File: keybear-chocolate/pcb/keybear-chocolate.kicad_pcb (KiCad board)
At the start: 2 copper layers, 136.9 x 98.2 mm, 97 parts, among them J1 MJ-4PP-9, J2 BATT, J3 LED, J4 OLED, SW1 SW_PUSH, SW10 SW_PUSH, SW11 SW_PUSH, SW12 SW_PUSH, SW13 SW_PUSH, SW14 SW_PUSH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

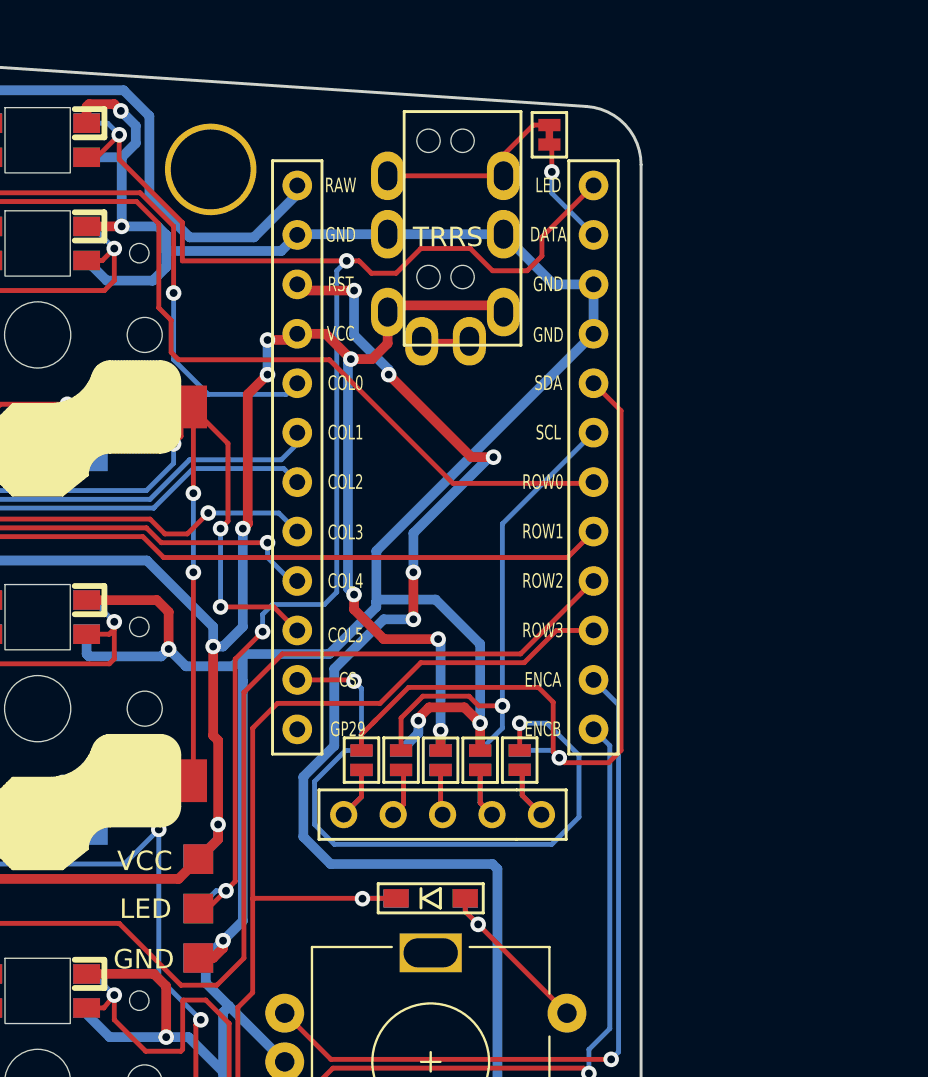
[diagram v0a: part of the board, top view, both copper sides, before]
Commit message: moving LED ping. Adding/rename RX/TX
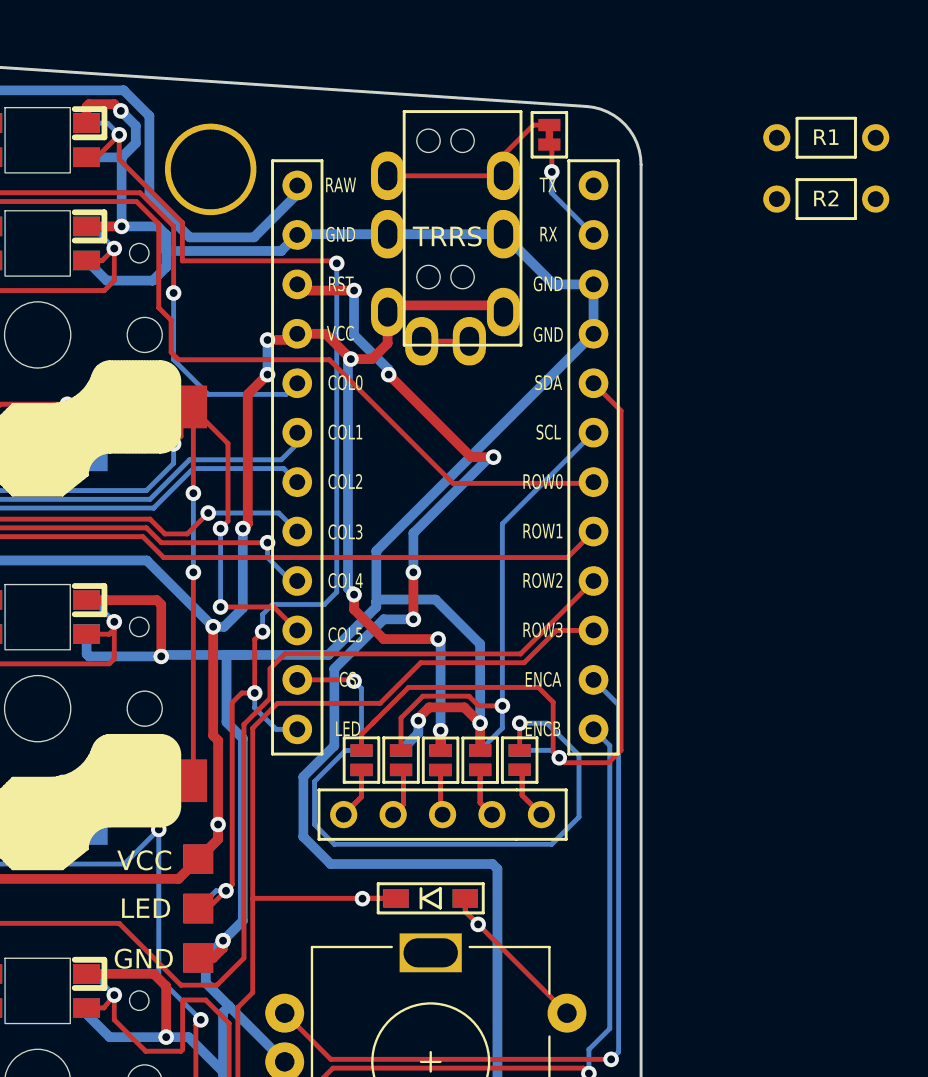
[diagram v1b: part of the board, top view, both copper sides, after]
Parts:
- added R1: R, SofleKeyboard-footprint:RESISTOR_mini, F.Cu at (286.5, 97.6)
- added R2: R, SofleKeyboard-footprint:RESISTOR_mini, F.Cu at (286.5, 100.7)
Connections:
- net data renamed RX
- U1 pad 1: LED -> TX
- U1 pad 13: unconnected-(U1-B6-Pad13) -> LED
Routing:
- net LED: track 77.4 -> 64.1 mm, vias 4 -> 5
- net VCC: track 875.4 -> 874.4 mm
- net GND: track 901.1 -> 901.9 mm

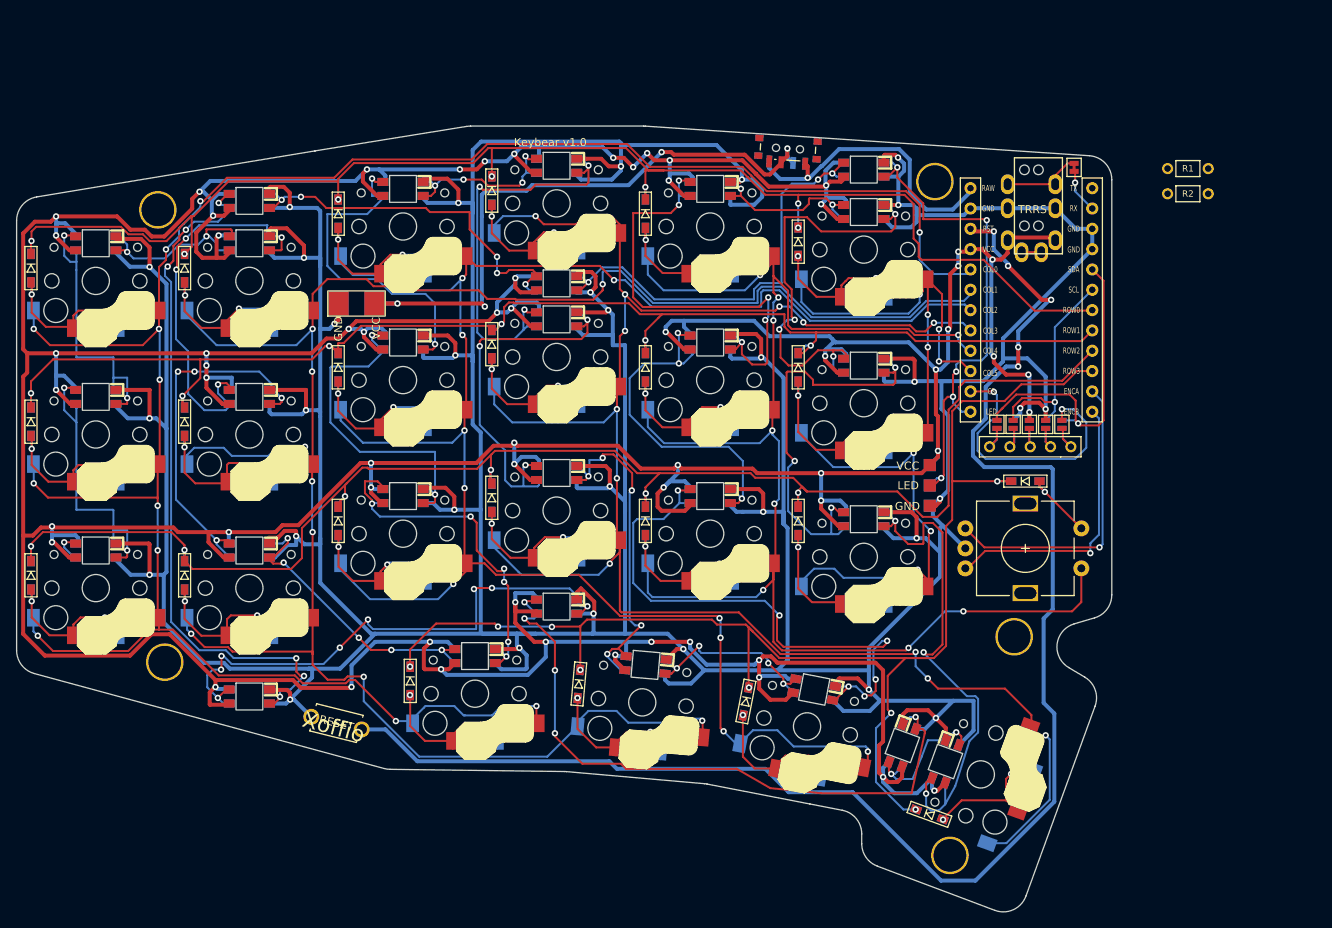
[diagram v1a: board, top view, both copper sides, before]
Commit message: board will be able to do uart or i2c communication between boards
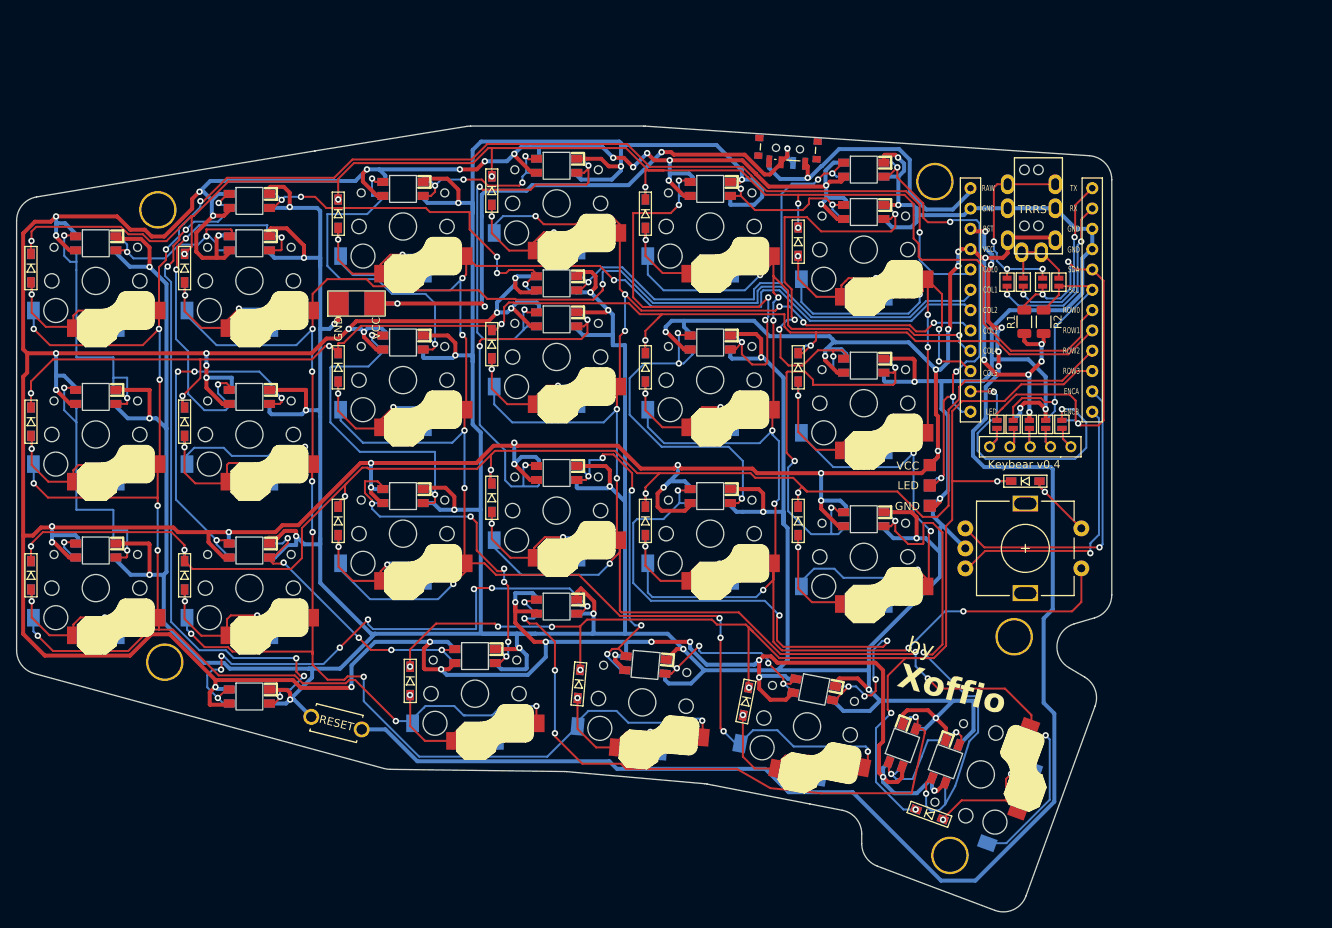
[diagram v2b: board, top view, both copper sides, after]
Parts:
- removed JP1: , kbd:JPC2
- added JP12: , kbd:Jumper, F.Cu at (263.9, 111.8)
- added JP13: , kbd:Jumper, F.Cu at (265.9, 111.8)
- added JP14: , kbd:Jumper, F.Cu at (268.4, 111.8)
- added JP15: , kbd:Jumper, F.Cu at (270.4, 111.8)
- R1, R2: footprint SofleKeyboard-footprint:RESISTOR_mini -> Resistor_SMD:R_1206_3216Metric
- moved R1 28.0 mm to (266.1, 116.7), turned to 90 degrees
- moved R2 24.1 mm to (268.5, 116.7), turned to 90 degrees
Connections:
- J1 pad A: unconnected-(J1-PadA) -> Net-(J1-PadA)
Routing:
- net TX: track 0.00 -> 22.0 mm, vias 0 -> 2
- net Net-(J1-PadB): track 10.0 -> 26.7 mm, vias 0 -> 3
- net RX: track 5.70 -> 22.3 mm, vias 1 -> 2
- net SDA: track 40.4 -> 55.9 mm, vias 1 -> 3
- net VCC: track 874.4 -> 884.6 mm, vias 61 -> 63
- net Net-(J1-PadA): track 0.00 -> 9.94 mm
- net row0: track 178.0 -> 187.3 mm
- net SCL: track 26.3 -> 34.4 mm
- net reset: track 192.1 -> 185.3 mm
- net GND: track 901.9 -> 907.3 mm
- net unconnected-(J1-PadA): track 2.45 -> 0.00 mm
- net LED: track 64.1 -> 61.7 mm
- net row1: track 173.0 -> 174.4 mm
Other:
- board text added: "Keybear v0.4"
- board text added: "by"

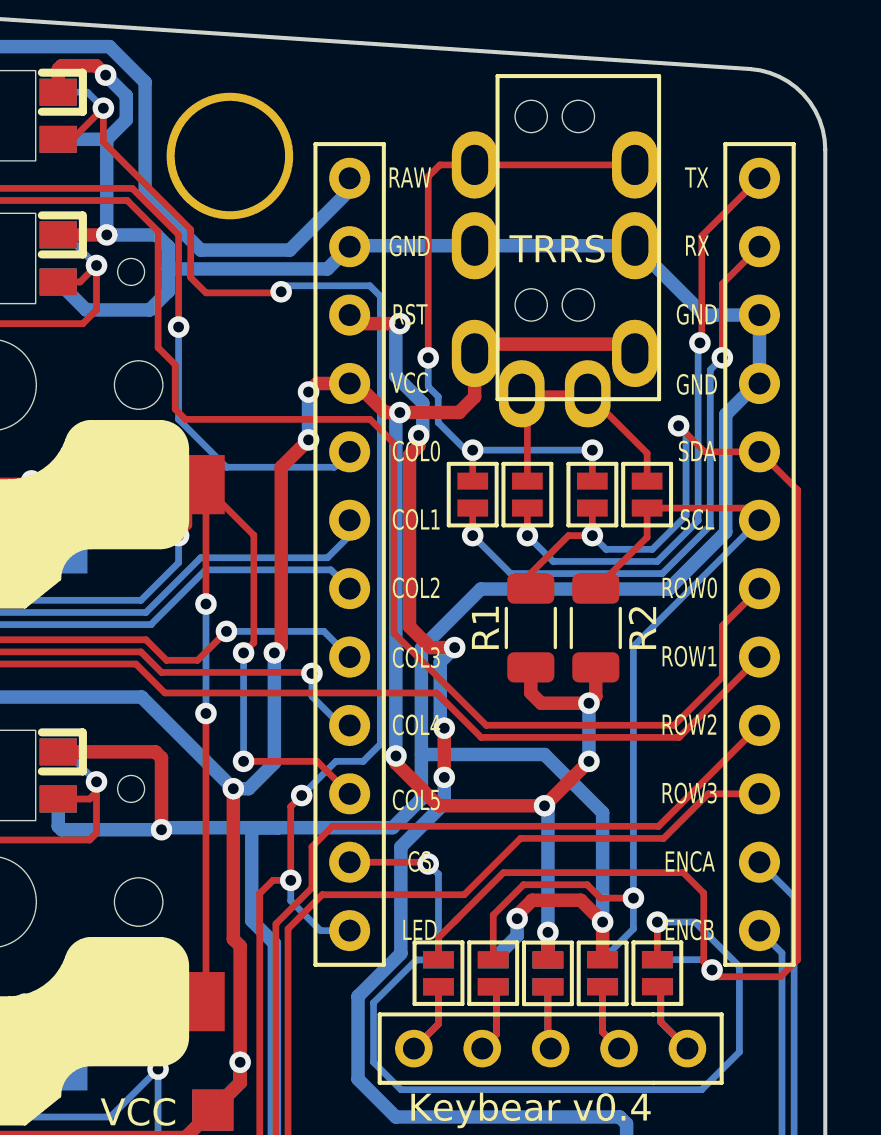
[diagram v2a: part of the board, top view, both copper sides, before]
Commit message: shift tracks around TRRS to start makind a modular mini-pcb
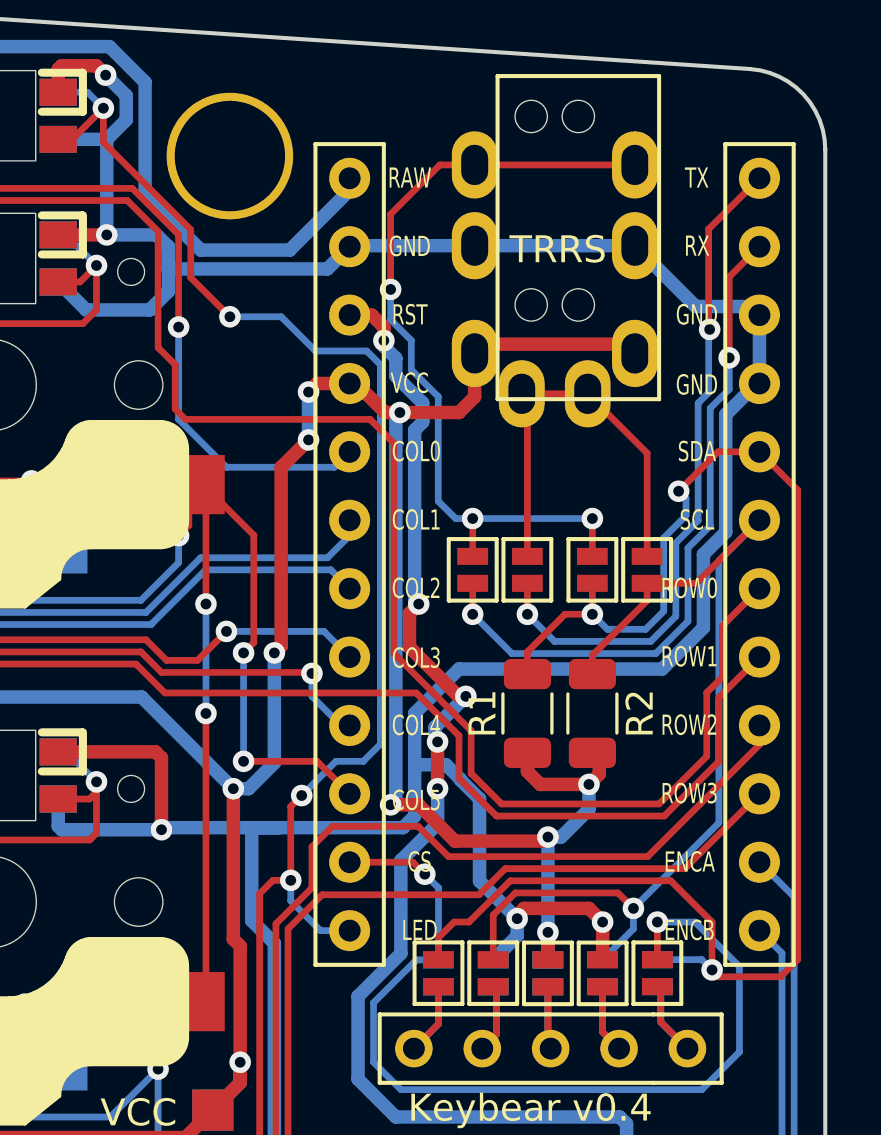
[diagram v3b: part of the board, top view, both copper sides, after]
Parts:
- moved R1 3.18 mm to (265.9, 119.9)
- moved R2 3.18 mm to (268.4, 119.9)
- moved JP12 2.79 mm to (263.9, 114.6)
- moved JP13 2.79 mm to (265.9, 114.6)
- moved JP14 2.79 mm to (268.4, 114.6)
- moved JP15 2.79 mm to (270.4, 114.6)
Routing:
- net Net-(J1-PadA): track 9.94 -> 15.5 mm
- net row0: track 187.3 -> 192.5 mm
- net row1: track 174.4 -> 179.1 mm
- net Net-(J1-PadB): track 26.7 -> 31.1 mm
- net GND: track 907.3 -> 903.9 mm
- net TX: track 22.0 -> 25.1 mm
- net RX: track 22.3 -> 25.3 mm
- net SCL: track 34.4 -> 36.2 mm
- net LED: track 61.7 -> 60.0 mm
- net row2: track 192.8 -> 194.1 mm
- net VCC: track 884.6 -> 883.6 mm, vias 63 -> 62
- net reset: track 185.3 -> 184.8 mm

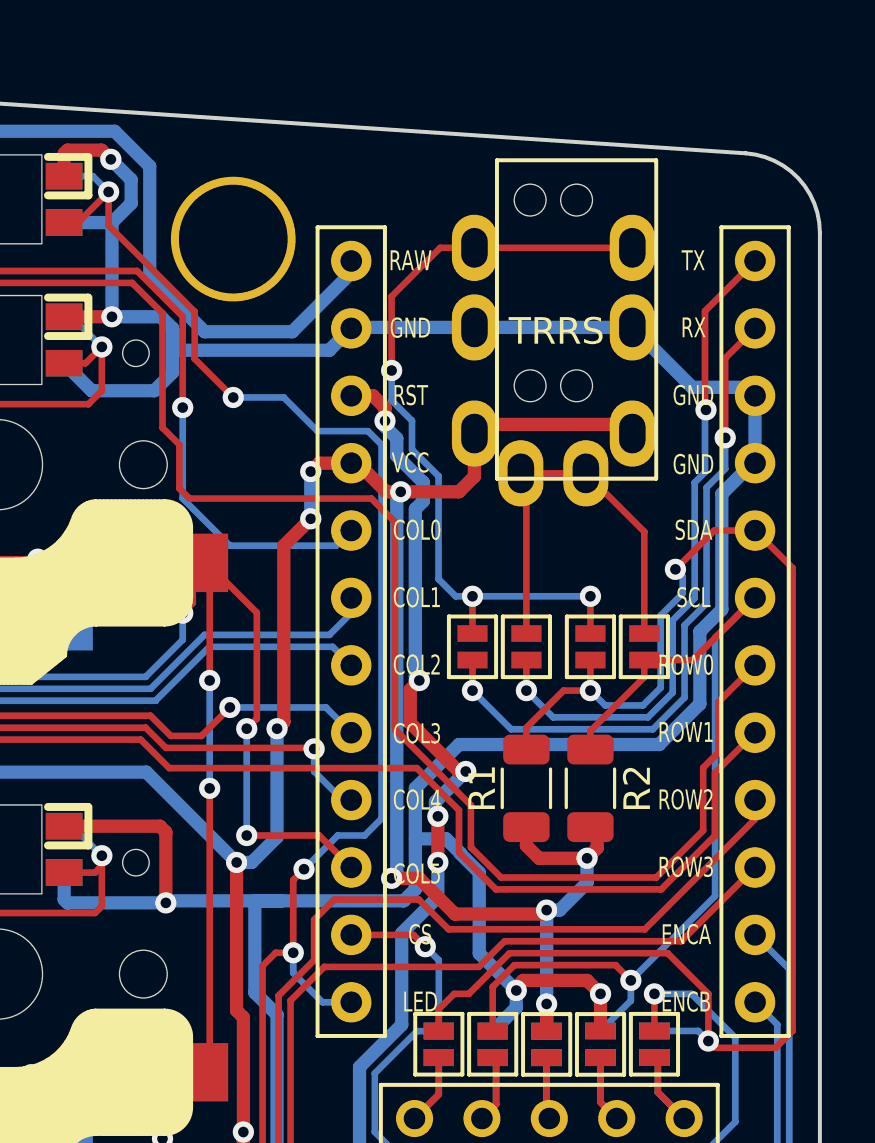
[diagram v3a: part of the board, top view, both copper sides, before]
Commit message: making space for the small pcb
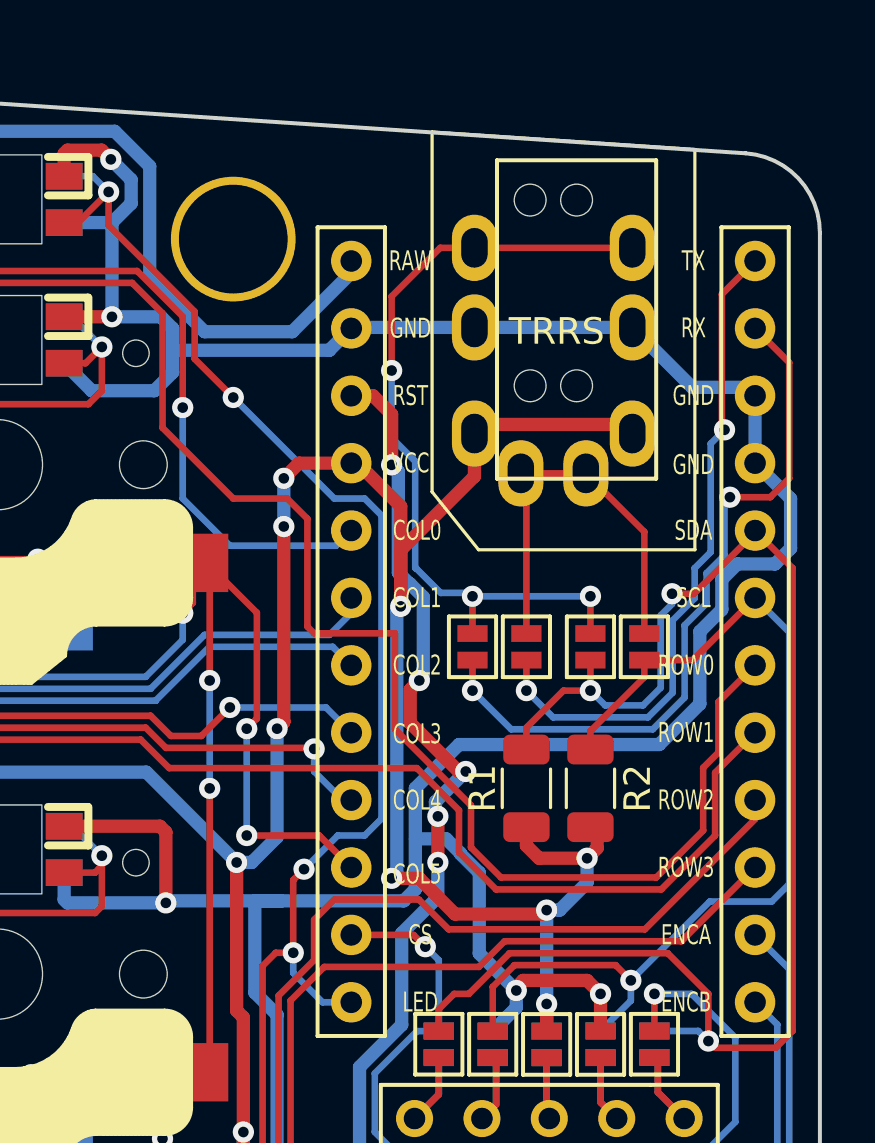
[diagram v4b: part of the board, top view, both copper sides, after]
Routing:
- net VCC: track 883.6 -> 886.8 mm
- net SCL: track 36.2 -> 38.6 mm
- net GND: track 903.9 -> 905.9 mm
- net RX: track 25.3 -> 27.2 mm
- net LED: track 60.0 -> 58.5 mm
- net row0: track 192.5 -> 191.5 mm
- net SDA: track 56.1 -> 55.4 mm
